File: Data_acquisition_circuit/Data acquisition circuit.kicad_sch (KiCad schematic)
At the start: 30 parts, among them U1 STM32F767VGTx

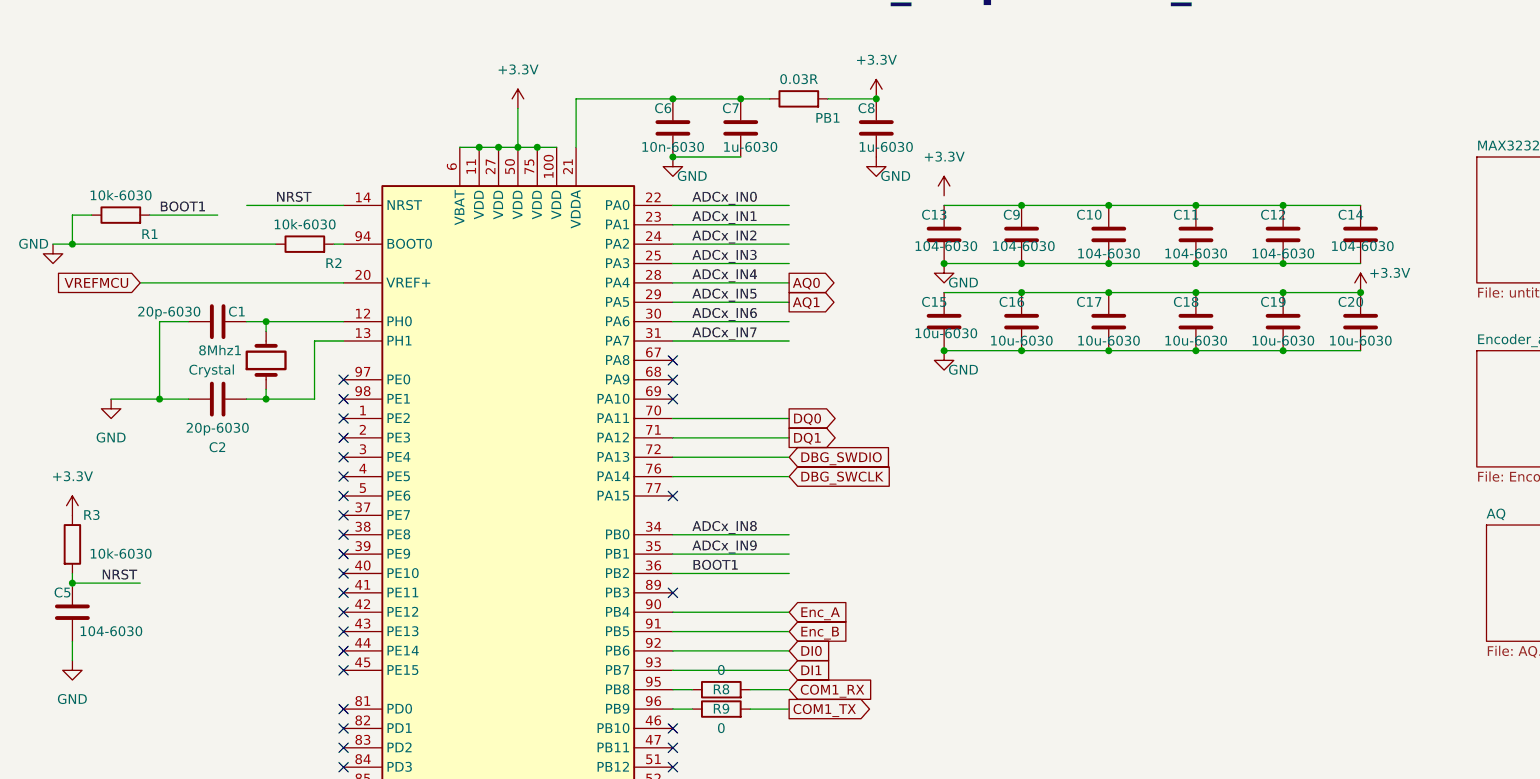
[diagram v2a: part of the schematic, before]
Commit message: covert 0603 to 0805
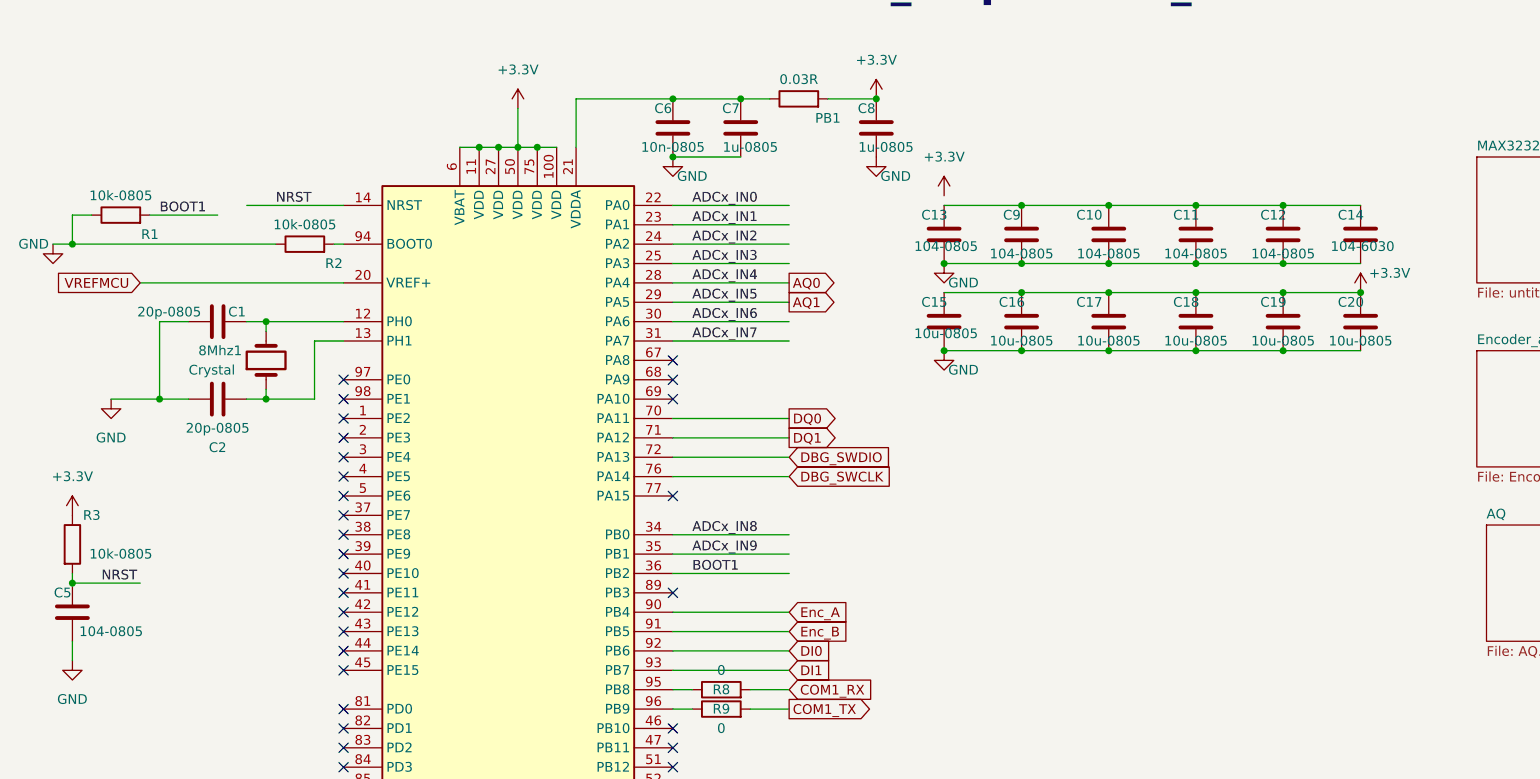
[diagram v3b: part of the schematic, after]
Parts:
- C1, C2: value 20p-6030 -> 20p-0805
- C10, C11, C12, C13, C5, C9: value 104-6030 -> 104-0805
- C15, C16, C17, C18, C19, C20: value 10u-6030 -> 10u-0805
- C6: value 10n-6030 -> 10n-0805
- C7, C8: value 1u-6030 -> 1u-0805
- R1, R2, R3: value 10k-6030 -> 10k-0805
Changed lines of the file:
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@@
       (effects (font (size 1.27 1.27)))
     )
-    (property "Value" "10u-6030" (at 171.45 69.85 0)
+    (property "Value" "10u-0805" (at 171.45 69.85 0)
       (effects (font (size 1.27 1.27)))
     )
@@
       (effects (font (size 1.27 1.27)))
     )
-    (property "Value" "10u-6030" (at 160.02 69.85 0)
+    (property "Value" "10u-0805" (at 160.02 69.85 0)
       (effects (font (size 1.27 1.27)))
     )
@@
       (effects (font (size 1.27 1.27)))
     )
-    (property "Value" "104-6030" (at 160.02 58.42 0)
+    (property "Value" "104-0805" (at 160.02 58.42 0)
       (effects (font (size 1.27 1.27)))
     )
@@
       (effects (font (size 1.27 1.27)))
     )
-    (property "Value" "20p-6030" (at 36.83 66.04 90)
+    (property "Value" "20p-0805" (at 36.83 66.04 90)
       (effects (font (size 1.27 1.27)))
     )
@@
       (effects (font (size 1.27 1.27)))
     )
-    (property "Value" "104-6030" (at 171.45 58.42 0)
+    (property "Value" "104-0805" (at 171.45 58.42 0)
       (effects (font (size 1.27 1.27)))
     )
@@
       (effects (font (size 1.27 1.27)))
     )
-    (property "Value" "10k-6030" (at 54.61 54.61 90)
+    (property "Value" "10k-0805" (at 54.61 54.61 90)
       (effects (font (size 1.27 1.27)))
     )
@@
       (effects (font (size 1.27 1.27)))
     )
-    (property "Value" "104-6030" (at 148.85 57.453 0)
+    (property "Value" "104-0805" (at 148.59 58.42 0)
       (effects (font (size 1.27 1.27)))
     )
@@
       (effects (font (size 1.27 1.27)))
     )
-    (property "Value" "10u-6030" (at 138.69 68.883 0)
+    (property "Value" "10u-0805" (at 138.69 68.883 0)
       (effects (font (size 1.27 1.27)))
     )
@@
       (effects (font (size 1.27 1.27)))
     )
-    (property "Value" "10k-6030" (at 30.48 97.79 0)
+    (property "Value" "10k-0805" (at 30.48 97.79 0)
       (effects (font (size 1.27 1.27)))
     )
@@
       (effects (font (size 1.27 1.27)))
     )
-    (property "Value" "104-6030" (at 138.69 57.453 0)
+    (property "Value" "104-0805" (at 138.69 57.453 0)
       (effects (font (size 1.27 1.27)))
     )
@@
       (effects (font (size 1.27 1.27)))
     )
-    (property "Value" "10u-6030" (at 182.88 69.85 0)
+    (property "Value" "10u-0805" (at 182.88 69.85 0)
       (effects (font (size 1.27 1.27)))
     )
@@
       (effects (font (size 1.27 1.27)))
     )
-    (property "Value" "10u-6030" (at 148.59 69.85 0)
+    (property "Value" "10u-0805" (at 148.59 69.85 0)
       (effects (font (size 1.27 1.27)))
     )
@@
       (effects (font (size 1.27 1.27)))
     )
-    (property "Value" "20p-6030" (at 43.18 81.28 90)
+    (property "Value" "20p-0805" (at 43.18 81.28 90)
       (effects (font (size 1.27 1.27)))
     )
@@
       (effects (font (size 1.27 1.27)))
     )
-    (property "Value" "10u-6030" (at 193.04 69.85 0)
+    (property "Value" "10u-0805" (at 193.04 69.85 0)
       (effects (font (size 1.27 1.27)))
     )
@@
       (effects (font (size 1.27 1.27)))
     )
-    (property "Value" "10n-6030" (at 102.87 44.45 0)
+    (property "Value" "10n-0805" (at 102.87 44.45 0)
       (effects (font (size 1.27 1.27)))
     )
@@
       (effects (font (size 1.27 1.27)))
     )
-    (property "Value" "10k-6030" (at 30.48 50.8 90)
+    (property "Value" "10k-0805" (at 30.48 50.8 90)
       (effects (font (size 1.27 1.27)))
     )
@@
       (effects (font (size 1.27 1.27)))
     )
-    (property "Value" "1u-6030" (at 130.81 44.45 0)
+    (property "Value" "1u-0805" (at 130.81 44.45 0)
       (effects (font (size 1.27 1.27)))
     )
@@
       (effects (font (size 1.27 1.27)))
     )
-    (property "Value" "104-6030" (at 182.88 58.42 0)
+    (property "Value" "104-0805" (at 182.88 58.42 0)
       (effects (font (size 1.27 1.27)))
     )
@@
       (effects (font (size 1.27 1.27)))
     )
-    (property "Value" "1u-6030" (at 113.03 44.45 0)
+    (property "Value" "1u-0805" (at 113.03 44.45 0)
       (effects (font (size 1.27 1.27)))
     )
@@
       (effects (font (size 1.27 1.27)))
     )
-    (property "Value" "104-6030" (at 29.21 107.95 0)
-      (effects (font (size 1.27 1.27)))
-    )
+    (property "Value" "104-0805" (at 29.21 107.95 0)
+      (effects (font (size 1.27 1.27)))
+    )

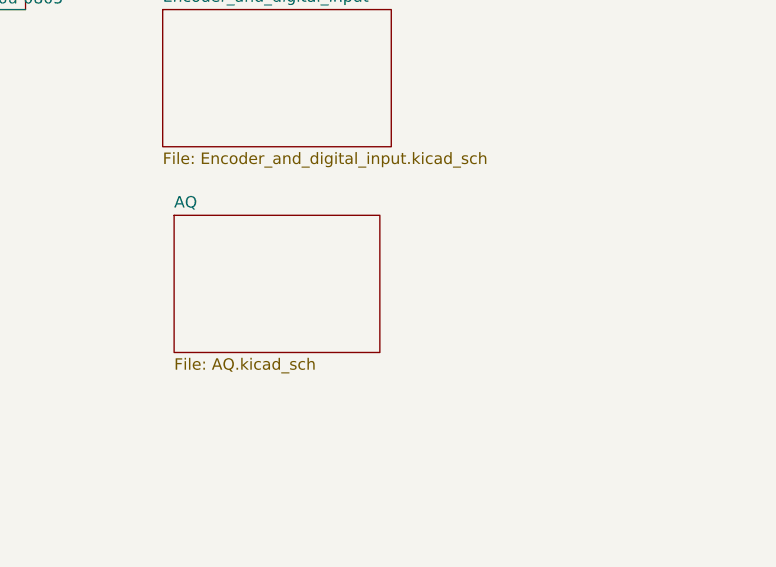
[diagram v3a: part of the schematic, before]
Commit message: add amplifier, adc and rewrite power file
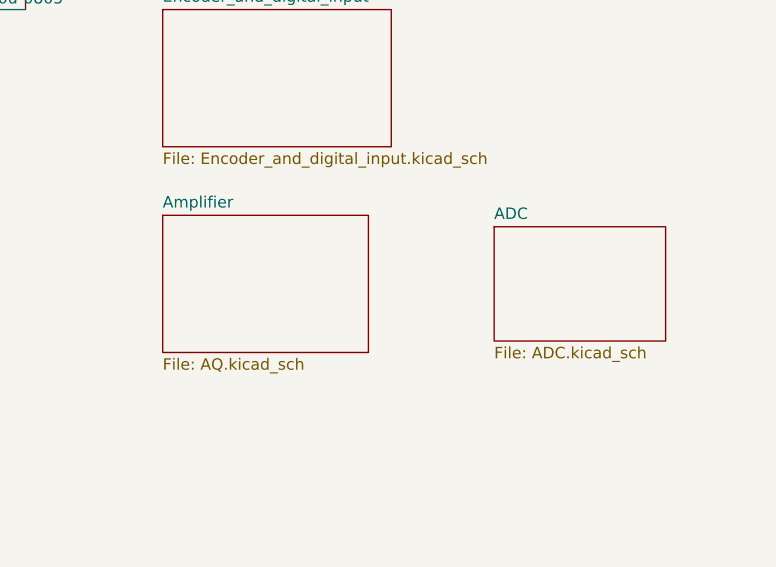
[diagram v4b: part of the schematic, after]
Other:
- sheet AQ renamed Amplifier
- added sheet ADC (ADC.kicad_sch)
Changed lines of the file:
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@@
     )
   )
-  (sheet (at 209.55 93.98) (size 22.86 15.24) (fields_autoplaced)
+  (sheet (at 245.11 95.25) (size 19.05 12.7) (fields_autoplaced)
     (stroke (width 0.1524) (type solid))
     (fill (color 0 0 0 0.0000))
-    (property "Sheetname" "AQ" (at 209.55 93.2684 0)
+    (property "Sheetname" "ADC" (at 245.11 94.5384 0)
       (effects (font (size 1.27 1.27)) (justify left bottom))
     )
-    (property "Sheetfile" "AQ.kicad_sch" (at 209.55 109.8046 0)
+    (property "Sheetfile" "ADC.kicad_sch" (at 245.11 108.5346 0)
       (effects (font (size 1.27 1.27)) (justify left top))
     )
+    (instances
+      (project "Data acquisition circuit"
+        (path "/1b7d87d8-ce09-4d95-b010-1b82030051eb" (page "6"))
+      )
+    )
+  )
+  (sheet (at 208.28 93.98) (size 22.86 15.24) (fields_autoplaced)
+    (stroke (width 0.1524) (type solid))
+    (fill (color 0 0 0 0.0000))
+    (property "Sheetname" "Amplifier" (at 208.28 93.2684 0)
+      (effects (font (size 1.27 1.27)) (justify left bottom))
+    )
+    (property "Sheetfile" "AQ.kicad_sch" (at 208.28 109.8046 0)
+      (effects (font (size 1.27 1.27)) (justify left top))
+    )
